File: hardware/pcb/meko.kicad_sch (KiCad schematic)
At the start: 0 parts

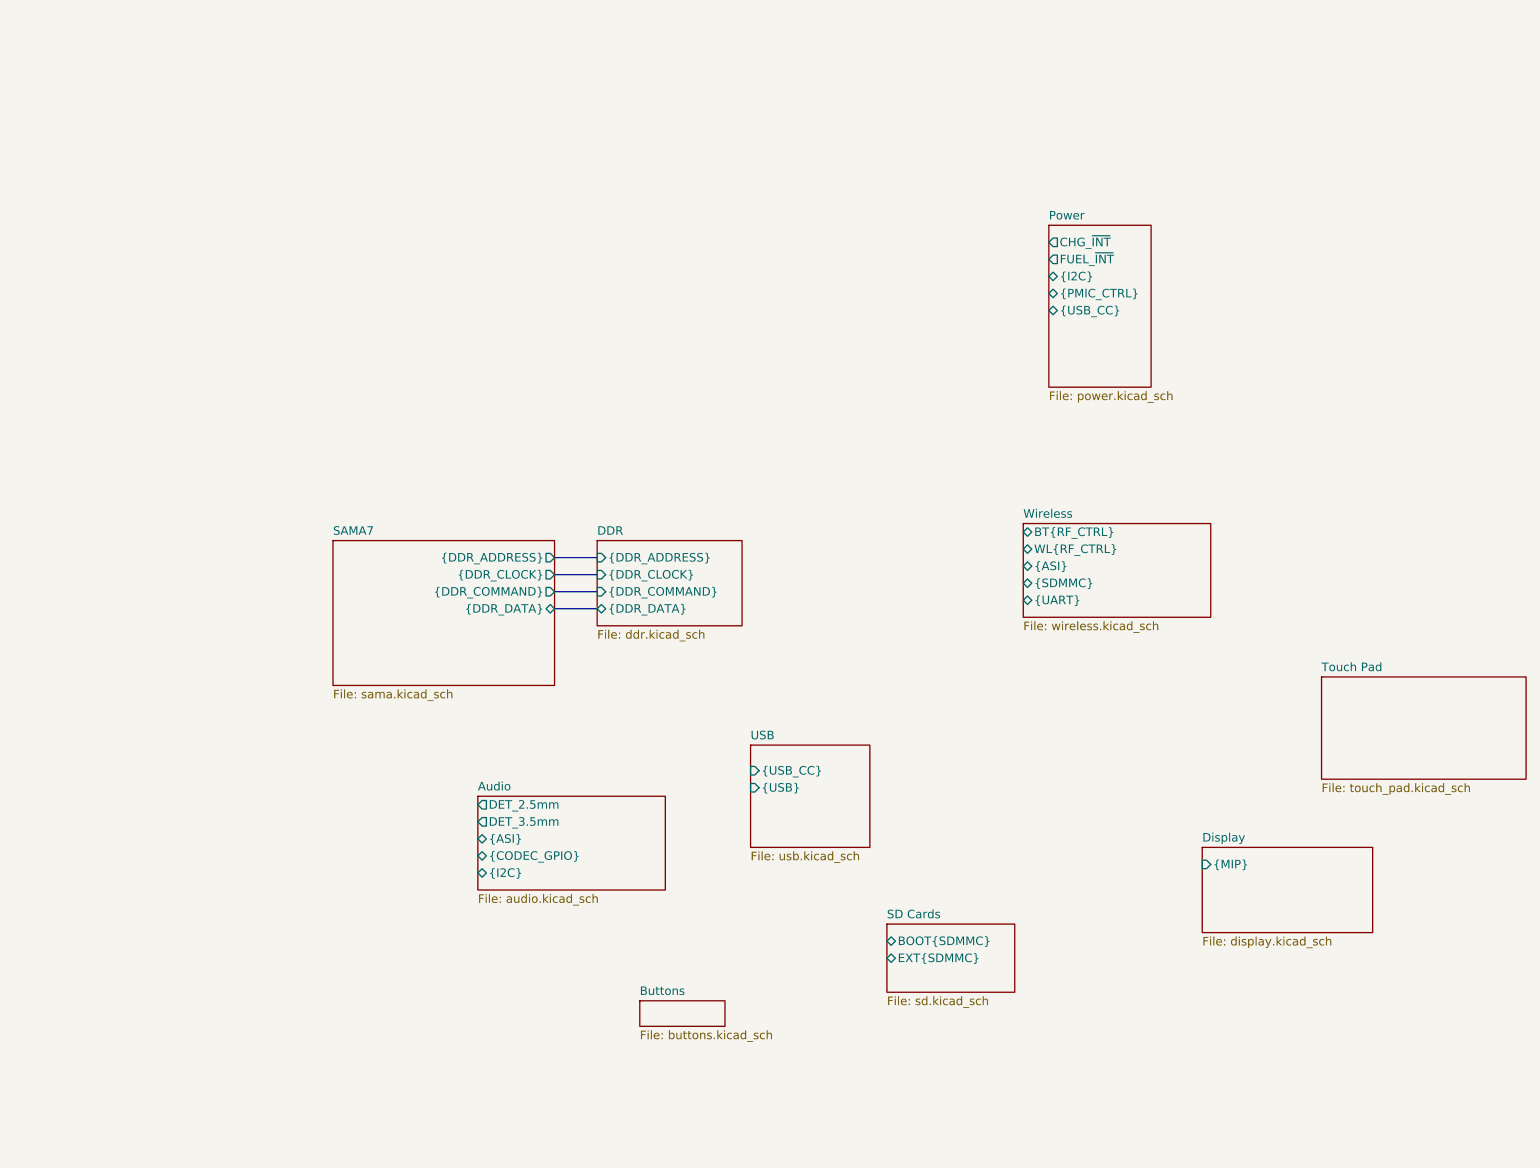
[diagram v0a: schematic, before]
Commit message: assigning pins
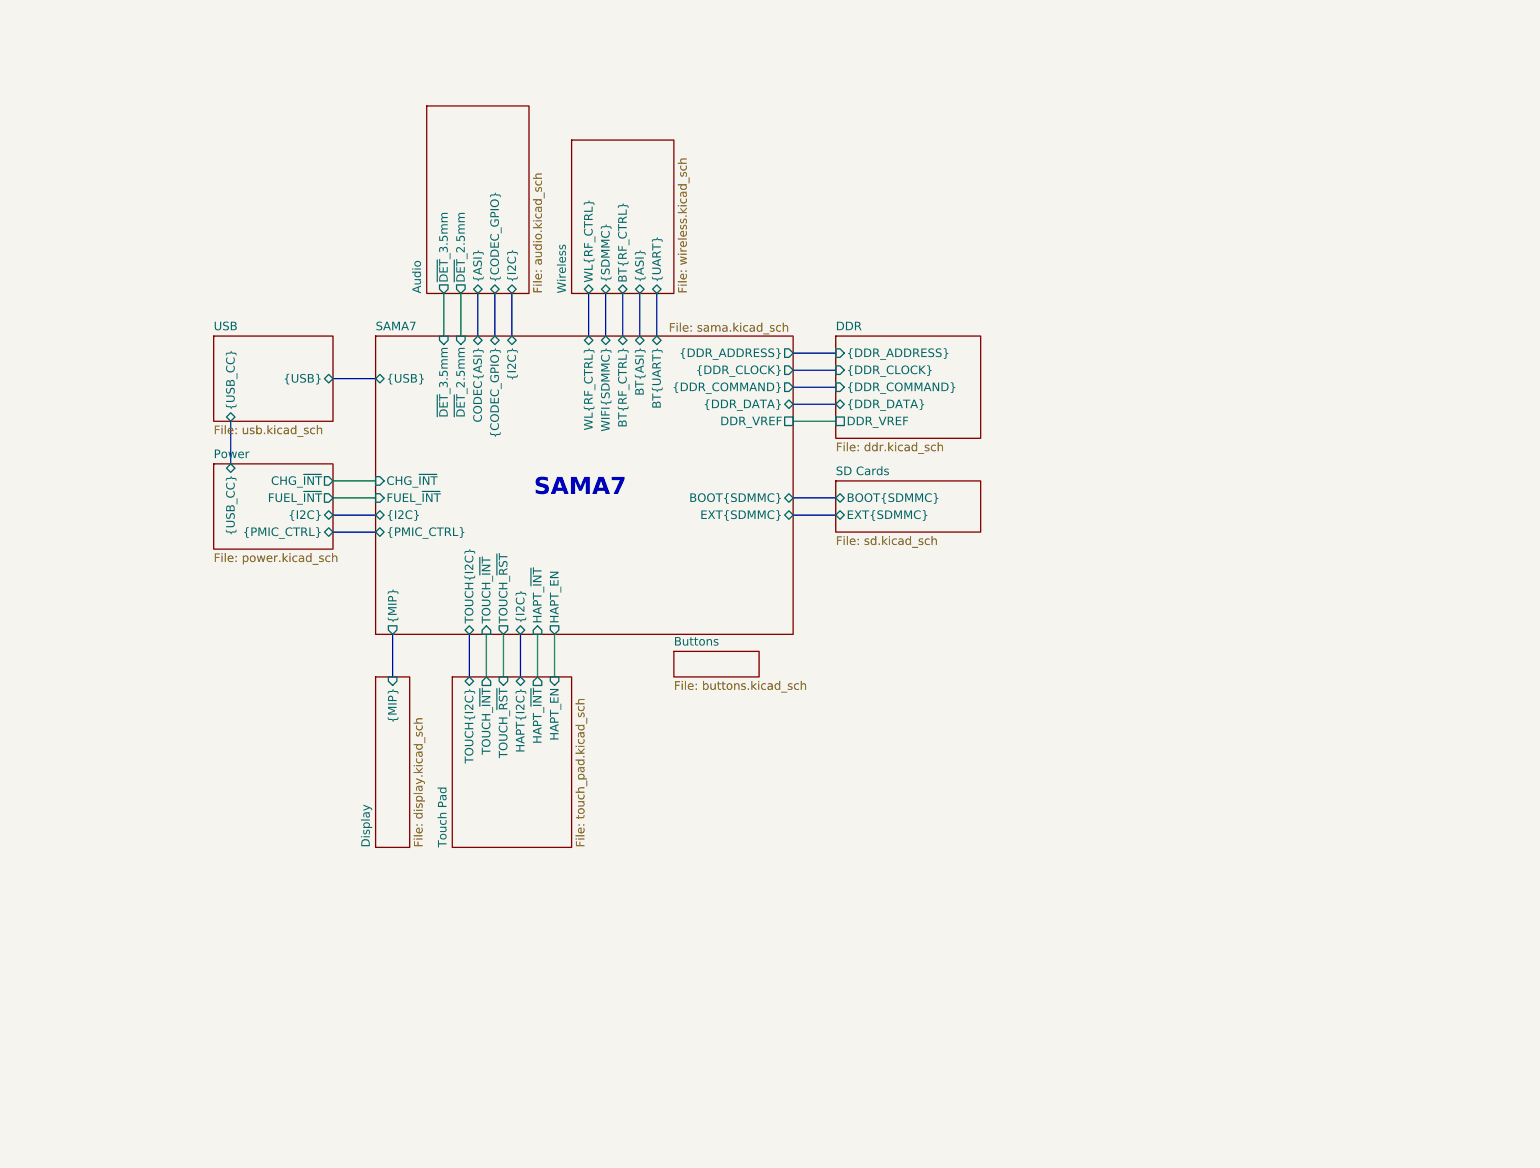
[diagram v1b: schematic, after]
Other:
- sheet Audio ports: added ~{DET}_2.5mm, ~{DET}_3.5mm; removed DET_2.5mm, DET_3.5mm
- sheet DDR ports: added DDR_VREF; removed none
- sheet SAMA7 ports: added BOOT{SDMMC}, BT{ASI}, BT{RF_CTRL}, BT{UART}, CHG_~{INT}, CODEC{ASI}, DDR_VREF, EXT{SDMMC}, FUEL_~{INT}, HAPT_EN, HAPT_~{INT}, TOUCH_~{INT}, TOUCH_~{RST}, TOUCH{I2C}, WIFI{SDMMC}, WL{RF_CTRL}, {CODEC_GPIO}, {I2C}, {MIP}, {PMIC_CTRL}, {USB}, ~{DET}_2.5mm, ~{DET}_3.5mm; removed none
- sheet Touch Pad ports: added HAPT_EN, HAPT_~{INT}, HAPT{I2C}, TOUCH_~{INT}, TOUCH_~{RST}, TOUCH{I2C}; removed none
- note added: "SAMA7"

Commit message: added buttons
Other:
- sheet Buttons ports: added {BUTTONS}; removed none
- sheet Power ports: added {BUTTONS}; removed none
- sheet SAMA7 ports: added {BUTTONS}; removed none
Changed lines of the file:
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@@
 		)
+	)
+	(junction
+		(at 69.85 104.14)
+		(diameter 0)
+		(color 0 0 0 0)
 	)
 	(wire
@@
 	(bus
 		(pts
+			(xy 49.53 104.14) (xy 69.85 104.14)
+		)
+		(stroke
+			(width 0)
+			(type default)
+		)
+	)
+	(bus
+		(pts
 			(xy 67.31 96.52) (xy 73.66 96.52)
 		)
@@
 	(bus
 		(pts
+			(xy 69.85 104.14) (xy 73.66 104.14)
+		)
+		(stroke
+			(width 0)
+			(type default)
+		)
+	)
+	(bus
+		(pts
 			(xy 93.98 63.5) (xy 93.98 69.85)
 		)
@@
 	(bus
 		(pts
+			(xy 69.85 104.14) (xy 69.85 110.49)
+		)
+		(stroke
+			(width 0)
+			(type default)
+		)
+	)
+	(bus
+		(pts
 			(xy 91.44 63.5) (xy 91.44 69.85)
 		)
@@
 		)
 	)
+	(bus
+		(pts
+			(xy 67.31 110.49) (xy 69.85 110.49)
+		)
+		(stroke
+			(width 0)
+			(type default)
+		)
+	)
 	(wire
 		(pts
@@
 		(pts
 			(xy 135.89 77.47) (xy 142.24 77.47)
+		)
+		(stroke
+			(width 0)
+			(type default)
+		)
+	)
+	(bus
+		(pts
+			(xy 49.53 101.6) (xy 49.53 104.14)
 		)
 		(stroke
@@
 			)
 		)
+		(pin "{BUTTONS}" input
+			(at 73.66 104.14 180)
+			(effects
+				(font
+					(size 1.27 1.27)
+				)
+				(justify left)
+			)
+		)
 		(instances
 			(project "meko"
@@
 	)
 	(sheet
-		(at 49.53 69.85)
-		(size 17.78 12.7)
+		(at 46.99 69.85)
+		(size 20.32 12.7)
 		(exclude_from_sim no)
 		(in_bom yes)
@@
 		)
 		(property "Sheetname" "USB"
-			(at 49.53 69.1384 0)
+			(at 46.99 69.1384 0)
 			(show_name no)
 			(do_not_autoplace no)
@@
 		)
 		(property "Sheetfile" "usb.kicad_sch"
-			(at 49.53 83.1346 0)
+			(at 46.99 83.1346 0)
 			(show_name no)
 			(do_not_autoplace no)
@@
 	)
 	(sheet
-		(at 49.53 88.9)
-		(size 17.78 12.7)
+		(at 46.99 88.9)
+		(size 20.32 12.7)
 		(exclude_from_sim no)
 		(in_bom yes)
 		(on_board yes)
 		(dnp no)
-		(fields_autoplaced yes)
 		(stroke
 			(width 0.1524)
@@
 		)
 		(property "Sheetname" "Power"
-			(at 49.53 88.1884 0)
+			(at 46.99 88.1884 0)
 			(show_name no)
 			(do_not_autoplace no)
@@
 		)
 		(property "Sheetfile" "power.kicad_sch"
-			(at 49.53 102.1846 0)
+			(at 50.292 102.108 0)
 			(show_name no)
 			(do_not_autoplace no)
@@
 				)
 				(justify right)
+			)
+		)
+		(pin "{BUTTONS}" input
+			(at 49.53 101.6 270)
+			(effects
+				(font
+					(size 1.27 1.27)
+				)
+				(justify left)
 			)
 		)
@@
 	)
 	(sheet
-		(at 118.11 116.84)
-		(size 12.7 3.81)
+		(at 46.99 107.95)
+		(size 20.32 5.08)
 		(exclude_from_sim no)
 		(in_bom yes)
@@
 		)
 		(property "Sheetname" "Buttons"
-			(at 118.11 116.1284 0)
+			(at 46.99 107.2384 0)
 			(show_name no)
 			(do_not_autoplace no)
@@
 		)
 		(property "Sheetfile" "buttons.kicad_sch"
-			(at 118.11 121.2346 0)
+			(at 46.99 113.6146 0)
 			(show_name no)
 			(do_not_autoplace no)
@@
 			)
 		)
+		(pin "{BUTTONS}" output
+			(at 67.31 110.49 0)
+			(effects
+				(font
+					(size 1.27 1.27)
+				)
+				(justify right)
+			)
+		)

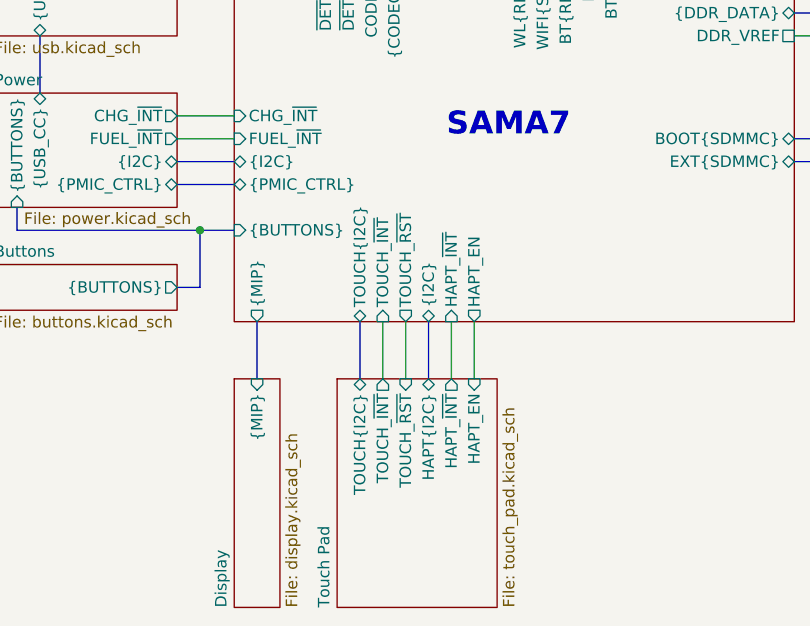
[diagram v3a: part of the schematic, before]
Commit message: main board: removed touch_rst label
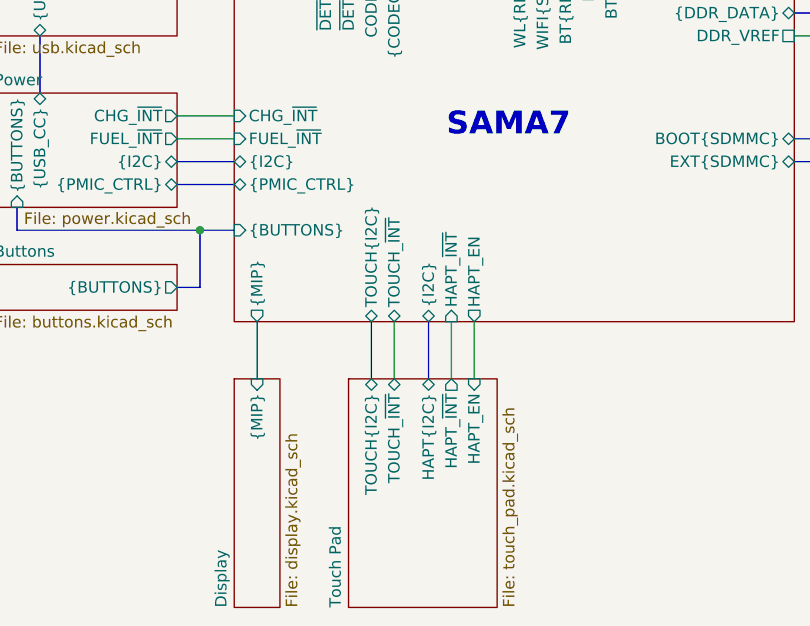
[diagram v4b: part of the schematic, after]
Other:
- sheet SAMA7 ports: added none; removed TOUCH_~{RST}
- sheet Touch Pad ports: added none; removed TOUCH_~{RST}
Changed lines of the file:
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@@
 	(bus
 		(pts
-			(xy 125.73 119.38) (xy 125.73 125.73)
+			(xy 127 119.38) (xy 127 125.73)
 		)
 		(stroke
@@
 	(wire
 		(pts
-			(xy 128.27 119.38) (xy 128.27 125.73)
+			(xy 129.54 119.38) (xy 129.54 125.73)
 		)
 		(stroke
@@
 		(pts
 			(xy 105.41 115.57) (xy 107.95 115.57)
-		)
-		(stroke
-			(width 0)
-			(type default)
-		)
-	)
-	(wire
-		(pts
-			(xy 130.81 119.38) (xy 130.81 125.73)
 		)
 		(stroke
@@
 			)
 		)
-		(pin "TOUCH_~{INT}" input
-			(at 128.27 119.38 270)
-			(effects
-				(font
-					(size 1.27 1.27)
-				)
-				(justify left)
-			)
-		)
-		(pin "TOUCH_~{RST}" output
-			(at 130.81 119.38 270)
+		(pin "TOUCH_~{INT}" bidirectional
+			(at 129.54 119.38 270)
 			(effects
 				(font
@@
 		)
 		(pin "TOUCH{I2C}" bidirectional
-			(at 125.73 119.38 270)
+			(at 127 119.38 270)
 			(effects
 				(font
@@
 	)
 	(sheet
-		(at 123.19 125.73)
-		(size 17.78 25.4)
+		(at 124.46 125.73)
+		(size 16.51 25.4)
 		(exclude_from_sim no)
 		(in_bom yes)
@@
 		)
 		(property "Sheetname" "Touch Pad"
-			(at 122.4784 151.13 90)
+			(at 123.7484 151.13 90)
 			(show_name no)
 			(do_not_autoplace no)
@@
 			)
 		)
-		(pin "TOUCH_~{INT}" output
-			(at 128.27 125.73 90)
-			(effects
-				(font
-					(size 1.27 1.27)
-				)
-				(justify right)
-			)
-		)
-		(pin "TOUCH_~{RST}" input
-			(at 130.81 125.73 90)
+		(pin "TOUCH_~{INT}" bidirectional
+			(at 129.54 125.73 90)
 			(effects
 				(font
@@
 		)
 		(pin "TOUCH{I2C}" bidirectional
-			(at 125.73 125.73 90)
-			(effects
-				(font
+			(at 127 125.73 90)
+			(effects
+				(font

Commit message: started cleaning up schematic
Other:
- sheet Touch Pad renamed Touchpad
- sheet Touchpad: file touch_pad.kicad_sch -> touchpad.kicad_sch
- company: (none) -> Gensis
- title: (none) -> Power
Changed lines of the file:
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@@
 	(generator_version "10.0")
 	(paper "A4")
+	(title_block
+		(title "Power")
+		(rev "v1.0.0")
+		(company "Gensis")
+	)
 	(text "SAMA7"
 		(exclude_from_sim no)
@@
 			(color 0 0 0 0)
 		)
-		(property "Sheetname" "Touch Pad"
+		(property "Sheetname" "Touchpad"
 			(at 123.7484 151.13 90)
 			(show_name no)
@@
 			)
 		)
-		(property "Sheetfile" "touch_pad.kicad_sch"
+		(property "Sheetfile" "touchpad.kicad_sch"
 			(at 141.5546 151.13 90)
 			(show_name no)

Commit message: mainboard: finished touchpad schematic
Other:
- sheet SAMA7 ports: added none; removed HAPT_~{INT}
- sheet Touchpad ports: added none; removed HAPT_~{INT}
- title: Power -> Overview
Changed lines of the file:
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@@
 	(paper "A4")
 	(title_block
-		(title "Power")
+		(title "Overview")
 		(rev "v1.0.0")
 		(company "Gensis")
@@
 	(wire
 		(pts
-			(xy 138.43 119.38) (xy 138.43 125.73)
+			(xy 135.89 119.38) (xy 135.89 125.73)
 		)
 		(stroke
@@
 	(wire
 		(pts
-			(xy 135.89 119.38) (xy 135.89 125.73)
+			(xy 124.46 68.58) (xy 124.46 74.93)
+		)
+		(stroke
+			(width 0)
+			(type default)
+		)
+	)
+	(bus
+		(pts
+			(xy 133.35 119.38) (xy 133.35 125.73)
+		)
+		(stroke
+			(width 0)
+			(type default)
+		)
+	)
+	(bus
+		(pts
+			(xy 146.05 68.58) (xy 146.05 74.93)
+		)
+		(stroke
+			(width 0)
+			(type default)
+		)
+	)
+	(bus
+		(pts
+			(xy 173.99 85.09) (xy 180.34 85.09)
+		)
+		(stroke
+			(width 0)
+			(type default)
+		)
+	)
+	(bus
+		(pts
+			(xy 173.99 77.47) (xy 180.34 77.47)
+		)
+		(stroke
+			(width 0)
+			(type default)
+		)
+	)
+	(bus
+		(pts
+			(xy 107.95 109.22) (xy 111.76 109.22)
+		)
+		(stroke
+			(width 0)
+			(type default)
+		)
+	)
+	(bus
+		(pts
+			(xy 132.08 68.58) (xy 132.08 74.93)
+		)
+		(stroke
+			(width 0)
+			(type default)
+		)
+	)
+	(bus
+		(pts
+			(xy 127 119.38) (xy 127 125.73)
 		)
 		(stroke
@@
 	(wire
 		(pts
-			(xy 124.46 68.58) (xy 124.46 74.93)
-		)
-		(stroke
-			(width 0)
-			(type default)
-		)
-	)
-	(bus
-		(pts
-			(xy 133.35 119.38) (xy 133.35 125.73)
-		)
-		(stroke
-			(width 0)
-			(type default)
-		)
-	)
-	(bus
-		(pts
-			(xy 146.05 68.58) (xy 146.05 74.93)
-		)
-		(stroke
-			(width 0)
-			(type default)
-		)
-	)
-	(bus
-		(pts
-			(xy 173.99 85.09) (xy 180.34 85.09)
-		)
-		(stroke
-			(width 0)
-			(type default)
-		)
-	)
-	(bus
-		(pts
-			(xy 173.99 77.47) (xy 180.34 77.47)
-		)
-		(stroke
-			(width 0)
-			(type default)
-		)
-	)
-	(bus
-		(pts
-			(xy 107.95 109.22) (xy 111.76 109.22)
-		)
-		(stroke
-			(width 0)
-			(type default)
-		)
-	)
-	(bus
-		(pts
-			(xy 132.08 68.58) (xy 132.08 74.93)
-		)
-		(stroke
-			(width 0)
-			(type default)
-		)
-	)
-	(bus
-		(pts
-			(xy 127 119.38) (xy 127 125.73)
+			(xy 105.41 99.06) (xy 111.76 99.06)
+		)
+		(stroke
+			(width 0)
+			(type default)
+		)
+	)
+	(bus
+		(pts
+			(xy 90.17 87.63) (xy 90.17 93.98)
+		)
+		(stroke
+			(width 0)
+			(type default)
+		)
+	)
+	(bus
+		(pts
+			(xy 151.13 68.58) (xy 151.13 74.93)
+		)
+		(stroke
+			(width 0)
+			(type default)
+		)
+	)
+	(bus
+		(pts
+			(xy 127 68.58) (xy 127 74.93)
 		)
 		(stroke
@@
 	(wire
 		(pts
-			(xy 105.41 99.06) (xy 111.76 99.06)
-		)
-		(stroke
-			(width 0)
-			(type default)
-		)
-	)
-	(bus
-		(pts
-			(xy 90.17 87.63) (xy 90.17 93.98)
-		)
-		(stroke
-			(width 0)
-			(type default)
-		)
-	)
-	(bus
-		(pts
-			(xy 151.13 68.58) (xy 151.13 74.93)
-		)
-		(stroke
-			(width 0)
-			(type default)
-		)
-	)
-	(bus
-		(pts
-			(xy 127 68.58) (xy 127 74.93)
+			(xy 121.92 68.58) (xy 121.92 74.93)
 		)
 		(stroke
@@
 	(wire
 		(pts
-			(xy 121.92 68.58) (xy 121.92 74.93)
-		)
-		(stroke
-			(width 0)
-			(type default)
-		)
-	)
-	(wire
-		(pts
 			(xy 129.54 119.38) (xy 129.54 125.73)
 		)
@@
 	)
 	(sheet
-		(at 119.38 40.64)
-		(size 15.24 27.94)
+		(at 119.38 45.72)
+		(size 15.24 22.86)
 		(exclude_from_sim no)
 		(in_bom yes)
@@
 		)
 		(pin "HAPT_EN" output
-			(at 138.43 119.38 270)
-			(effects
-				(font
-					(size 1.27 1.27)
-				)
-				(justify left)
-			)
-		)
-		(pin "HAPT_~{INT}" input
 			(at 135.89 119.38 270)
 			(effects
@@
 	(sheet
 		(at 124.46 125.73)
-		(size 16.51 25.4)
+		(size 13.97 25.4)
 		(exclude_from_sim no)
 		(in_bom yes)
@@
 		)
 		(property "Sheetfile" "touchpad.kicad_sch"
-			(at 141.5546 151.13 90)
+			(at 139.0146 151.13 90)
 			(show_name no)
 			(do_not_autoplace no)
@@
 		)
 		(pin "HAPT_EN" input
-			(at 138.43 125.73 90)
-			(effects
-				(font
-					(size 1.27 1.27)
-				)
-				(justify right)
-			)
-		)
-		(pin "HAPT_~{INT}" output
 			(at 135.89 125.73 90)
 			(effects

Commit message: routing
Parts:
- added H1, H2, H3, H4: MountingHole, MountingHole:MountingHole_2.2mm_M2, symbol Mechanical:MountingHole

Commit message: added silkscreen
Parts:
- added SYM1: Logo_Open_Hardware_Large, Symbol:OSHW-Logo2_9.8x8mm_SilkScreen, symbol Graphic:Logo_Open_Hardware_Large
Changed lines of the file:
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@@
+	)
+	(symbol
+		(lib_id "Graphic:Logo_Open_Hardware_Large")
+		(at 31.75 33.02 0)
+		(unit 1)
+		(body_style 1)
+		(exclude_from_sim no)
+		(in_bom no)
+		(on_board yes)
+		(in_pos_files yes)
+		(dnp no)
+		(fields_autoplaced yes)
+		(property "Reference" "SYM1"
+			(at 31.75 20.32 0)
+			(hide yes)
+			(show_name no)
+			(do_not_autoplace no)
+			(effects
+				(font
+					(size 1.27 1.27)
+				)
+			)
+		)
+		(property "Value" "Logo_Open_Hardware_Large"
+			(at 31.75 43.18 0)
+			(hide yes)
+			(show_name no)
+			(do_not_autoplace no)
+			(effects
+				(font
+					(size 1.27 1.27)
+				)
+			)
+		)
+		(property "Footprint" "Symbol:OSHW-Logo2_9.8x8mm_SilkScreen"
+			(at 31.75 33.02 0)
+			(hide yes)
+			(show_name no)
+			(do_not_autoplace no)
+			(effects
+				(font
+					(size 1.27 1.27)
+				)
+			)
+		)
+		(property "Datasheet" ""
+			(at 31.75 33.02 0)
+			(hide yes)
+			(show_name no)
+			(do_not_autoplace no)
+			(effects
+				(font
+					(size 1.27 1.27)
+				)
+			)
+		)
+		(property "Description" "Open Hardware logo, large"
+			(at 31.75 33.02 0)
+			(hide yes)
+			(show_name no)
+			(do_not_autoplace no)
+			(effects
+				(font
+					(size 1.27 1.27)
+				)
+			)
+		)
+		(property "Sim.Enable" "0"
+			(at 31.75 33.02 0)
+			(hide yes)
+			(show_name no)
+			(do_not_autoplace no)
+			(effects
+				(font
+					(size 1.27 1.27)
+				)
+			)
+		)
+		(instances
+			(project "meko"
+				(path "/da54f10a-146b-4941-a9c7-55c7173bb101"
+					(reference "SYM1")
+					(unit 1)
+				)
+			)
+		)
 	)
 	(symbol
